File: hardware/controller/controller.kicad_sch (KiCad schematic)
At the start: 0 parts

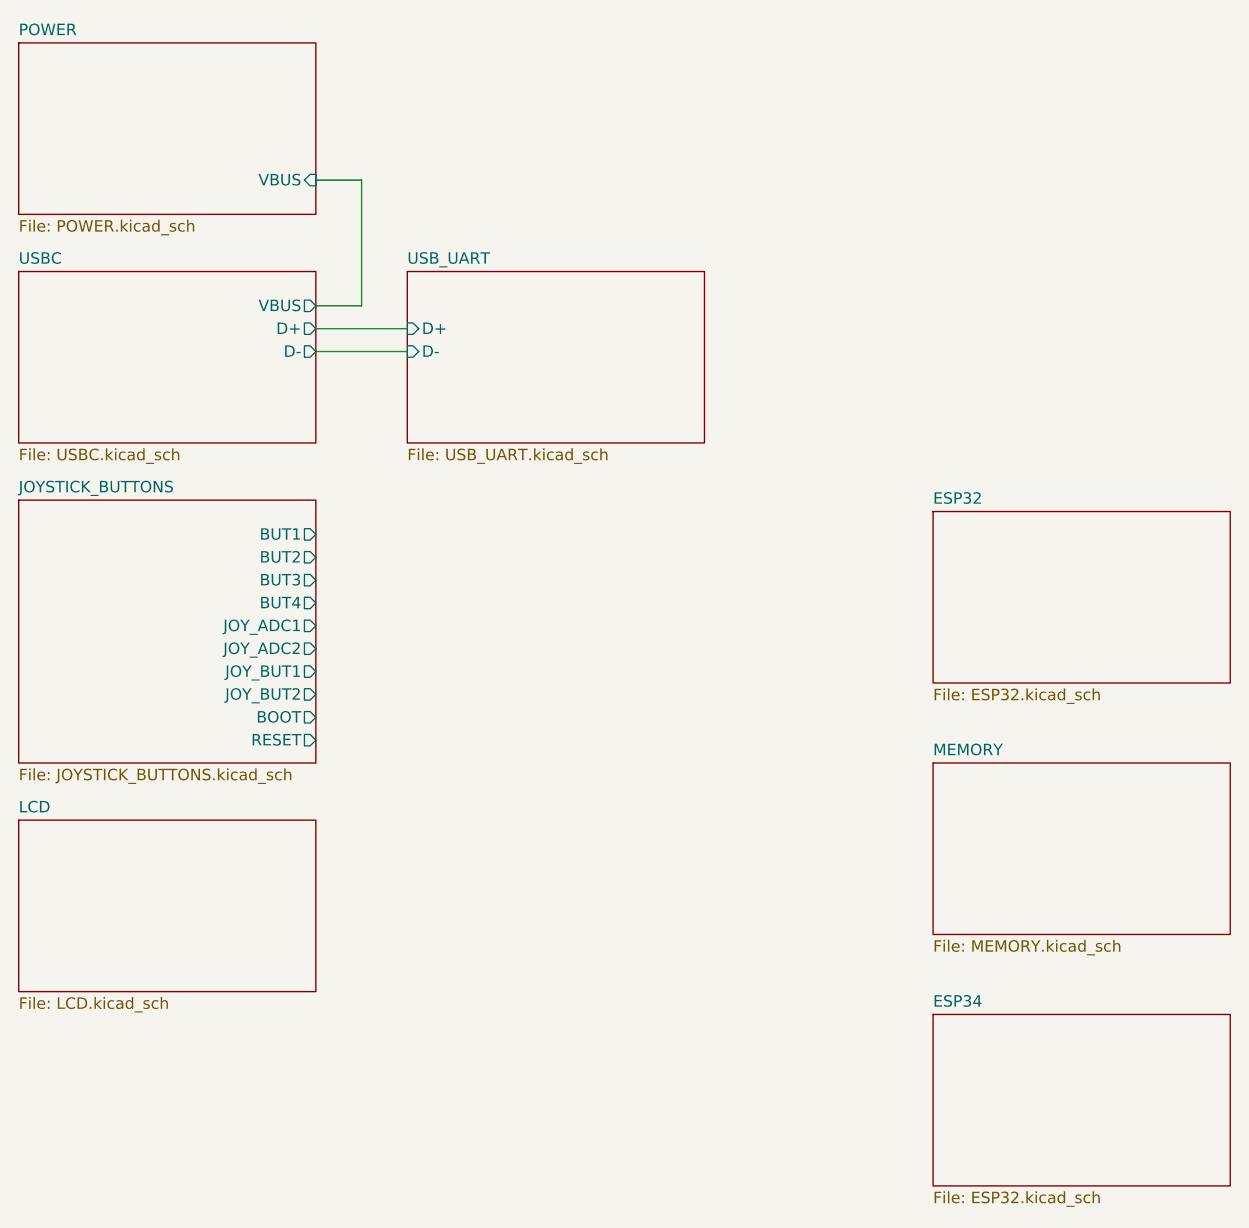
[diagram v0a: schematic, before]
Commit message: added LED IC's and USB UART bridge
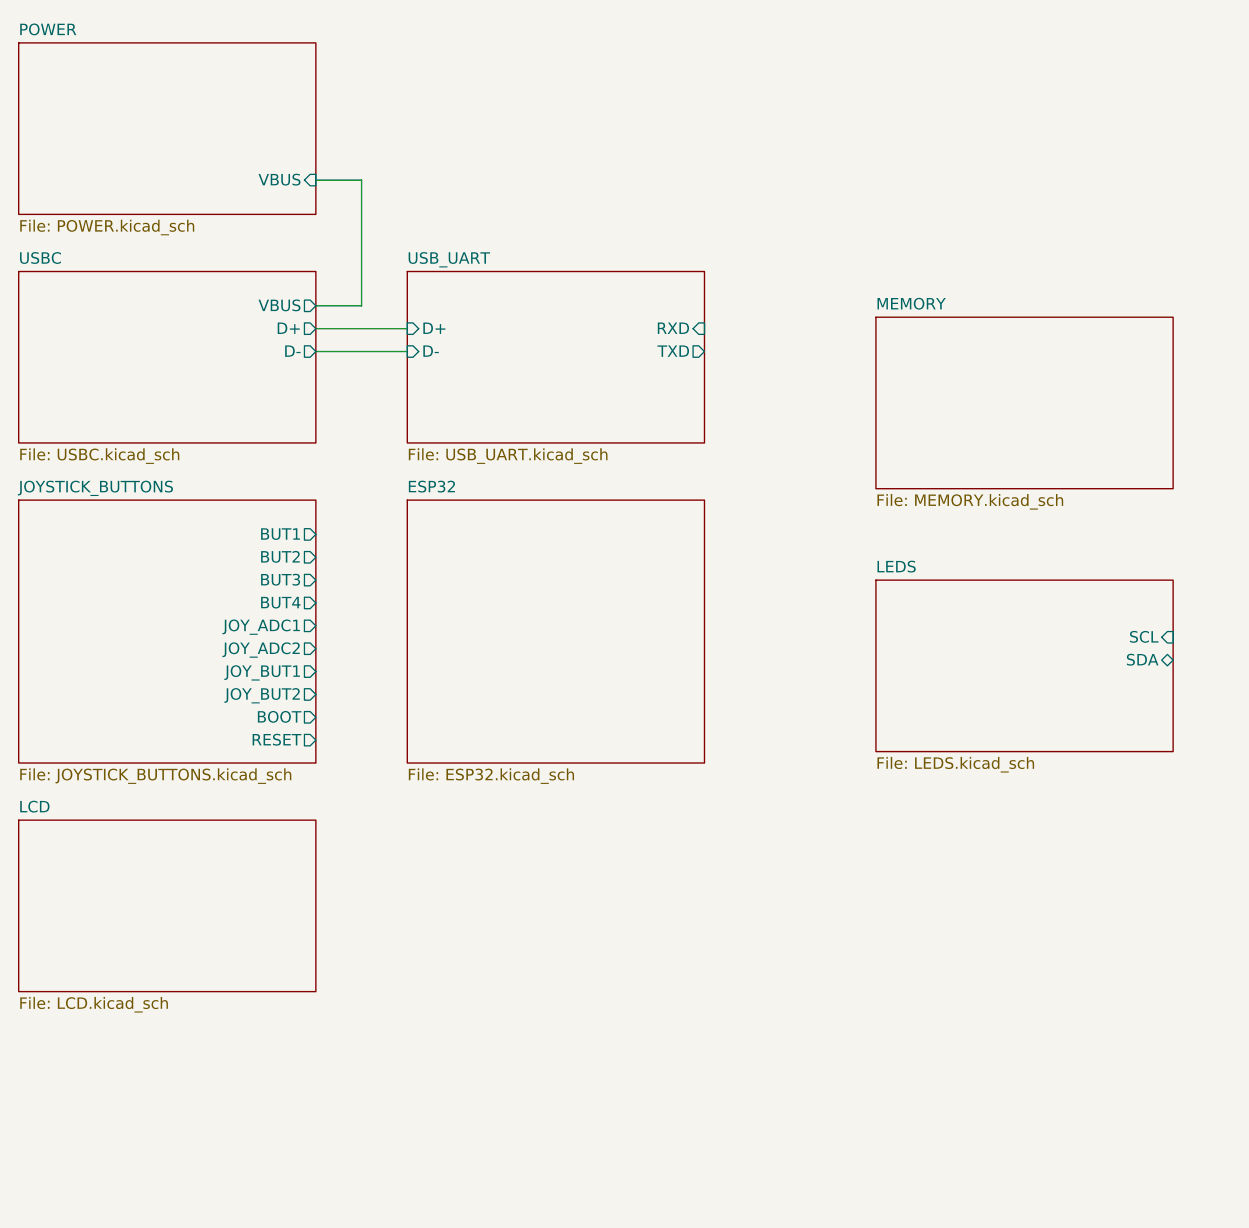
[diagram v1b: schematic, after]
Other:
- removed sheet ESP34
- added sheet LEDS (LEDS.kicad_sch)
- sheet USB_UART ports: added RXD, TXD; removed none
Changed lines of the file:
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@@
 	)
 	(sheet
-		(at 160.02 115.57)
+		(at 153.67 66.04)
 		(size 33.02 19.05)
 		(exclude_from_sim no)
@@
 		)
 		(property "Sheetname" "MEMORY"
-			(at 160.02 114.8584 0)
+			(at 153.67 65.3284 0)
 			(effects
 				(font
@@
 		)
 		(property "Sheetfile" "MEMORY.kicad_sch"
-			(at 160.02 135.2046 0)
+			(at 153.67 85.6746 0)
 			(effects
 				(font
@@
 				(path "/869bea87-c885-4ead-826b-3f34ceacafad"
 					(page "8")
+				)
+			)
+		)
+	)
+	(sheet
+		(at 153.67 95.25)
+		(size 33.02 19.05)
+		(exclude_from_sim no)
+		(in_bom yes)
+		(on_board yes)
+		(dnp no)
+		(fields_autoplaced yes)
+		(stroke
+			(width 0.1524)
+			(type solid)
+		)
+		(fill
+			(color 0 0 0 0.0000)
+		)
+		(property "Sheetname" "LEDS"
+			(at 153.67 94.5384 0)
+			(effects
+				(font
+					(size 1.27 1.27)
+				)
+				(justify left bottom)
+			)
+		)
+		(property "Sheetfile" "LEDS.kicad_sch"
+			(at 153.67 114.8846 0)
+			(effects
+				(font
+					(size 1.27 1.27)
+				)
+				(justify left top)
+			)
+		)
+		(pin "SCL" input
+			(at 186.69 101.6 0)
+			(effects
+				(font
+					(size 1.27 1.27)
+				)
+				(justify right)
+			)
+		)
+		(pin "SDA" bidirectional
+			(at 186.69 104.14 0)
+			(effects
+				(font
+					(size 1.27 1.27)
+				)
+				(justify right)
+			)
+		)
+		(instances
+			(project "controller"
+				(path "/869bea87-c885-4ead-826b-3f34ceacafad"
+					(page "9")
 				)
 			)
@@
 			)
 		)
+		(pin "RXD" input
+			(at 134.62 67.31 0)
+			(effects
+				(font
+					(size 1.27 1.27)
+				)
+				(justify right)
+			)
+		)
+		(pin "TXD" output
+			(at 134.62 69.85 0)
+			(effects
+				(font
+					(size 1.27 1.27)
+				)
+				(justify right)
+			)
+		)
 		(instances
 			(project "controller"
@@
 	)
 	(sheet
-		(at 160.02 87.63)
-		(size 33.02 19.05)
+		(at 101.6 86.36)
+		(size 33.02 29.21)
 		(exclude_from_sim no)
 		(in_bom yes)
@@
 		)
 		(property "Sheetname" "ESP32"
-			(at 160.02 86.9184 0)
+			(at 101.6 85.6484 0)
 			(effects
 				(font
@@
 		)
 		(property "Sheetfile" "ESP32.kicad_sch"
-			(at 160.02 107.2646 0)
+			(at 101.6 116.1546 0)
 			(effects
 				(font
@@
 				)
 			)
-		)
-	)
-	(sheet
-		(at 160.02 143.51)
-		(size 33.02 19.05)
-		(exclude_from_sim no)
-		(in_bom yes)
-		(on_board yes)
-		(dnp no)
-		(fields_autoplaced yes)
-		(stroke
-			(width 0.1524)
-			(type solid)
-		)
-		(fill
-			(color 0 0 0 0.0000)
-		)
-		(property "Sheetname" "ESP34"
-			(at 160.02 142.7984 0)
-			(effects
-				(font
-					(size 1.27 1.27)
-				)
-				(justify left bottom)
-			)
-		)
-		(property "Sheetfile" "ESP32.kicad_sch"
-			(at 160.02 163.1446 0)
-			(effects
-				(font
-					(size 1.27 1.27)
-				)
-				(justify left top)
-			)
-		)
-		(instances
-			(project "controller"
-				(path "/869bea87-c885-4ead-826b-3f34ceacafad"
-					(page "9")
-				)
-			)

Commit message: asdasd
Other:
- sheet JOYSTICK_BUTTONS ports: added BUT_BOOT, BUT_DWN, BUT_LFT, BUT_RHT, BUT_RST, BUT_UP, JOY1_H, JOY1_V, JOY2_H, JOY2_V; removed BOOT, BUT1, BUT2, BUT3, BUT4, JOY_ADC1, JOY_ADC2, JOY_BUT1, JOY_BUT2, RESET
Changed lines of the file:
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@@
 				)
 				(justify left top)
+				(hide yes)
 			)
 		)
@@
 				)
 				(justify left top)
+				(hide yes)
 			)
 		)
 		(pin "SCL" input
-			(at 186.69 101.6 0)
-			(effects
-				(font
-					(size 1.27 1.27)
-				)
-				(justify right)
+			(at 153.67 100.33 180)
+			(effects
+				(font
+					(size 1.27 1.27)
+				)
+				(justify left)
 			)
 		)
 		(pin "SDA" bidirectional
-			(at 186.69 104.14 0)
-			(effects
-				(font
-					(size 1.27 1.27)
-				)
-				(justify right)
+			(at 153.67 102.87 180)
+			(effects
+				(font
+					(size 1.27 1.27)
+				)
+				(justify left)
 			)
 		)
@@
 				)
 				(justify left top)
-			)
-		)
-		(pin "BUT1" output
-			(at 91.44 90.17 0)
-			(effects
-				(font
-					(size 1.27 1.27)
-				)
-				(justify right)
-			)
-		)
-		(pin "BUT2" output
-			(at 91.44 92.71 0)
-			(effects
-				(font
-					(size 1.27 1.27)
-				)
-				(justify right)
-			)
-		)
-		(pin "BUT3" output
-			(at 91.44 95.25 0)
-			(effects
-				(font
-					(size 1.27 1.27)
-				)
-				(justify right)
-			)
-		)
-		(pin "BUT4" output
-			(at 91.44 97.79 0)
-			(effects
-				(font
-					(size 1.27 1.27)
-				)
-				(justify right)
-			)
-		)
-		(pin "JOY_ADC1" output
-			(at 91.44 100.33 0)
-			(effects
-				(font
-					(size 1.27 1.27)
-				)
-				(justify right)
-			)
-		)
-		(pin "JOY_ADC2" output
-			(at 91.44 102.87 0)
-			(effects
-				(font
-					(size 1.27 1.27)
-				)
-				(justify right)
-			)
-		)
-		(pin "JOY_BUT1" output
-			(at 91.44 105.41 0)
-			(effects
-				(font
-					(size 1.27 1.27)
-				)
-				(justify right)
-			)
-		)
-		(pin "JOY_BUT2" output
-			(at 91.44 107.95 0)
-			(effects
-				(font
-					(size 1.27 1.27)
-				)
-				(justify right)
-			)
-		)
-		(pin "BOOT" output
-			(at 91.44 110.49 0)
-			(effects
-				(font
-					(size 1.27 1.27)
-				)
-				(justify right)
-			)
-		)
-		(pin "RESET" output
-			(at 91.44 113.03 0)
+				(hide yes)
+			)
+		)
+		(pin "BUT_BOOT" output
+			(at 91.44 91.44 0)
+			(effects
+				(font
+					(size 1.27 1.27)
+				)
+				(justify right)
+			)
+		)
+		(pin "BUT_DWN" output
+			(at 91.44 96.52 0)
+			(effects
+				(font
+					(size 1.27 1.27)
+				)
+				(justify right)
+			)
+		)
+		(pin "BUT_LFT" output
+			(at 91.44 99.06 0)
+			(effects
+				(font
+					(size 1.27 1.27)
+				)
+				(justify right)
+			)
+		)
+		(pin "BUT_RHT" output
+			(at 91.44 101.6 0)
+			(effects
+				(font
+					(size 1.27 1.27)
+				)
+				(justify right)
+			)
+		)
+		(pin "BUT_RST" output
+			(at 91.44 88.9 0)
+			(effects
+				(font
+					(size 1.27 1.27)
+				)
+				(justify right)
+			)
+		)
+		(pin "BUT_UP" output
+			(at 91.44 93.98 0)
+			(effects
+				(font
+					(size 1.27 1.27)
+				)
+				(justify right)
+			)
+		)
+		(pin "JOY1_H" output
+			(at 91.44 104.14 0)
+			(effects
+				(font
+					(size 1.27 1.27)
+				)
+				(justify right)
+			)
+		)
+		(pin "JOY1_V" output
+			(at 91.44 106.68 0)
+			(effects
+				(font
+					(size 1.27 1.27)
+				)
+				(justify right)
+			)
+		)
+		(pin "JOY2_H" output
+			(at 91.44 109.22 0)
+			(effects
+				(font
+					(size 1.27 1.27)
+				)
+				(justify right)
+			)
+		)
+		(pin "JOY2_V" output
+			(at 91.44 111.76 0)
 			(effects
 				(font
@@
 				)
 				(justify left top)
+				(hide yes)
 			)
 		)
@@
 				)
 				(justify left top)
+				(hide yes)
 			)
 		)
@@
 				)
 				(justify left top)
+				(hide yes)
 			)
 		)
@@
 	)
 	(sheet
-		(at 58.42 121.92)
+		(at 153.67 120.65)
 		(size 33.02 19.05)
 		(exclude_from_sim no)
@@
 		)
 		(property "Sheetname" "LCD"
-			(at 58.42 121.2084 0)
+			(at 153.67 119.9384 0)
 			(effects
 				(font
@@
 		)
 		(property "Sheetfile" "LCD.kicad_sch"
-			(at 58.42 141.5546 0)
-			(effects
-				(font
-					(size 1.27 1.27)
-				)
-				(justify left top)
+			(at 153.67 140.2846 0)
+			(effects
+				(font
+					(size 1.27 1.27)
+				)
+				(justify left top)
+				(hide yes)
 			)
 		)
@@
 				)
 				(justify left top)
-			)
-		)
+				(hide yes)
+			)
+		)

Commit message: a
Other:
- sheet ESP32 ports: added BUT_JOY{BUT_JOY_BUS}, DTR, RTS, RXD, SCL, SDA, TXD; removed none
- sheet JOYSTICK_BUTTONS ports: added BUT_JOY{BUT_JOY_BUS}; removed BUT_BOOT, BUT_DWN, BUT_LFT, BUT_RHT, BUT_RST, BUT_UP, JOY1_H, JOY1_V, JOY2_H, JOY2_V
- sheet LCD ports: added I2C_LCD, SPI_LCD; removed none
- sheet USBC ports: added USB+, USB-; removed D+, D-
- sheet USB_UART ports: added DTR, RTS, USB+, USB-, VBUS; removed D+, D-

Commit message: fixed bus stuff
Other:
- added sheet SPEAKER (SPEAKER.kicad_sch)
- sheet ESP32 ports: added I2C_CTP_LED{I2C_CTP_LED}, SPI_LCD_SD{SPI_LCD_SD}; removed SCL, SDA
- sheet LCD ports: added I2C_CTP_LED{I2C_CTP_LED}, SPI_LCD_SD{SPI_LCD_SD}; removed I2C_LCD, SPI_LCD
- sheet LEDS ports: added GPIO, I2C_CTP_LED{I2C_CTP_LED}; removed SCL, SDA
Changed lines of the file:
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@@
+	)
+	(junction
+		(at 151.13 105.41)
+		(diameter 0)
+		(color 0 0 0 0)
 	)
 	(junction
@@
 		(color 0 0 0 0)
 	)
+	(bus
+		(pts
+			(xy 151.13 105.41) (xy 151.13 120.65)
+		)
+		(stroke
+			(width 0)
+			(type default)
+		)
+	)
 	(wire
 		(pts
@@
 	(wire
 		(pts
-			(xy 134.62 96.52) (xy 154.94 96.52)
-		)
-		(stroke
-			(width 0)
-			(type default)
-		)
-	)
-	(wire
-		(pts
 			(xy 123.19 80.01) (xy 123.19 86.36)
 		)
@@
 		)
 	)
+	(bus
+		(pts
+			(xy 148.59 123.19) (xy 154.94 123.19)
+		)
+		(stroke
+			(width 0)
+			(type default)
+		)
+	)
+	(bus
+		(pts
+			(xy 154.94 100.33) (xy 151.13 100.33)
+		)
+		(stroke
+			(width 0)
+			(type default)
+		)
+	)
+	(bus
+		(pts
+			(xy 134.62 107.95) (xy 148.59 107.95)
+		)
+		(stroke
+			(width 0)
+			(type default)
+		)
+	)
 	(wire
 		(pts
@@
 		)
 	)
-	(wire
-		(pts
-			(xy 134.62 93.98) (xy 154.94 93.98)
-		)
-		(stroke
-			(width 0)
-			(type default)
-		)
-	)
 	(bus
 		(pts
@@
 		)
 	)
+	(bus
+		(pts
+			(xy 151.13 120.65) (xy 154.94 120.65)
+		)
+		(stroke
+			(width 0)
+			(type default)
+		)
+	)
+	(bus
+		(pts
+			(xy 148.59 107.95) (xy 148.59 123.19)
+		)
+		(stroke
+			(width 0)
+			(type default)
+		)
+	)
+	(bus
+		(pts
+			(xy 134.62 105.41) (xy 151.13 105.41)
+		)
+		(stroke
+			(width 0)
+			(type default)
+		)
+	)
 	(wire
 		(pts
@@
 		(pts
 			(xy 96.52 64.77) (xy 96.52 50.8)
+		)
+		(stroke
+			(width 0)
+			(type default)
+		)
+	)
+	(bus
+		(pts
+			(xy 151.13 100.33) (xy 151.13 105.41)
 		)
 		(stroke
@@
 			)
 		)
-		(pin "SCL" bidirectional
-			(at 154.94 93.98 180)
-			(effects
-				(font
-					(size 1.27 1.27)
-				)
-				(justify left)
-			)
-		)
-		(pin "SDA" bidirectional
-			(at 154.94 96.52 180)
+		(pin "GPIO" input
+			(at 154.94 97.79 180)
+			(effects
+				(font
+					(size 1.27 1.27)
+				)
+				(justify left)
+			)
+		)
+		(pin "I2C_CTP_LED{I2C_CTP_LED}" bidirectional
+			(at 154.94 100.33 180)
 			(effects
 				(font
@@
 			)
 		)
-		(pin "SCL" bidirectional
-			(at 134.62 93.98 0)
-			(effects
-				(font
-					(size 1.27 1.27)
-				)
-				(justify right)
-			)
-		)
-		(pin "SDA" bidirectional
-			(at 134.62 96.52 0)
-			(effects
-				(font
-					(size 1.27 1.27)
-				)
-				(justify right)
-			)
-		)
 		(pin "RXD" output
 			(at 125.73 86.36 90)
@@
 		(pin "DTR" input
 			(at 123.19 86.36 90)
+			(effects
+				(font
+					(size 1.27 1.27)
+				)
+				(justify right)
+			)
+		)
+		(pin "I2C_CTP_LED{I2C_CTP_LED}" bidirectional
+			(at 134.62 105.41 0)
+			(effects
+				(font
+					(size 1.27 1.27)
+				)
+				(justify right)
+			)
+		)
+		(pin "SPI_LCD_SD{SPI_LCD_SD}" bidirectional
+			(at 134.62 107.95 0)
 			(effects
 				(font
@@
 			)
 		)
-		(pin "I2C_LCD" bidirectional
-			(at 154.94 121.92 180)
-			(effects
-				(font
-					(size 1.27 1.27)
-				)
-				(justify left)
-			)
-		)
-		(pin "SPI_LCD" bidirectional
-			(at 154.94 125.73 180)
+		(pin "I2C_CTP_LED{I2C_CTP_LED}" bidirectional
+			(at 154.94 120.65 180)
+			(effects
+				(font
+					(size 1.27 1.27)
+				)
+				(justify left)
+			)
+		)
+		(pin "SPI_LCD_SD{SPI_LCD_SD}" bidirectional
+			(at 154.94 123.19 180)
 			(effects
 				(font
@@
 				)
 			)
+		)
+	)
+	(sheet
+		(at 58.42 120.65)
+		(size 33.02 21.59)
+		(exclude_from_sim no)
+		(in_bom yes)
+		(on_board yes)
+		(dnp no)
+		(fields_autoplaced yes)
+		(stroke
+			(width 0.1524)
+			(type solid)
+		)
+		(fill
+			(color 0 0 0 0.0000)
+		)
+		(property "Sheetname" "SPEAKER"
+			(at 58.42 119.9384 0)
+			(effects
+				(font
+					(size 1.27 1.27)
+				)
+				(justify left bottom)
+			)
+		)
+		(property "Sheetfile" "SPEAKER.kicad_sch"
+			(at 58.42 142.8246 0)
+			(effects
+				(font
+					(size 1.27 1.27)
+				)
+				(justify left top)
+			)
+		)
+		(instances
+			(project "controller"
+				(path "/869bea87-c885-4ead-826b-3f34ceacafad"
+					(page "10")
+				)
+			)

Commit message: bussin
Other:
- removed sheet SPEAKER
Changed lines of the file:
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@@
-	)
-	(sheet
-		(at 58.42 120.65)
-		(size 33.02 21.59)
-		(exclude_from_sim no)
-		(in_bom yes)
-		(on_board yes)
-		(dnp no)
-		(fields_autoplaced yes)
-		(stroke
-			(width 0.1524)
-			(type solid)
-		)
-		(fill
-			(color 0 0 0 0.0000)
-		)
-		(property "Sheetname" "SPEAKER"
-			(at 58.42 119.9384 0)
-			(effects
-				(font
-					(size 1.27 1.27)
-				)
-				(justify left bottom)
-			)
-		)
-		(property "Sheetfile" "SPEAKER.kicad_sch"
-			(at 58.42 142.8246 0)
-			(effects
-				(font
-					(size 1.27 1.27)
-				)
-				(justify left top)
-			)
-		)
-		(instances
-			(project "controller"
-				(path "/869bea87-c885-4ead-826b-3f34ceacafad"
-					(page "10")
-				)
-			)
-		)
 	)
 	(sheet

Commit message: added memory and fixed gpio pins
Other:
- sheet ESP32 ports: added LED_GPIO, MEM{MEMORY}; removed none
- sheet LEDS ports: added LED GPIO; removed GPIO
- sheet MEMORY ports: added MEM{MEMORY}; removed none
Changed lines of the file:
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@@
+	(bus
+		(pts
+			(xy 134.62 127) (xy 139.7 127)
+		)
+		(stroke
+			(width 0)
+			(type default)
+		)
+	)
 	(bus
 		(pts
@@
 		)
 	)
+	(bus
+		(pts
+			(xy 139.7 127) (xy 139.7 110.49)
+		)
+		(stroke
+			(width 0)
+			(type default)
+		)
+	)
 	(wire
 		(pts
@@
 		)
 	)
+	(wire
+		(pts
+			(xy 134.62 97.79) (xy 154.94 97.79)
+		)
+		(stroke
+			(width 0)
+			(type default)
+		)
+	)
 	(bus
 		(pts
@@
 		(pts
 			(xy 125.73 80.01) (xy 125.73 86.36)
+		)
+		(stroke
+			(width 0)
+			(type default)
+		)
+	)
+	(bus
+		(pts
+			(xy 139.7 110.49) (xy 134.62 110.49)
 		)
 		(stroke
@@
 	(sheet
 		(at 102.235 123.19)
-		(size 33.02 19.05)
+		(size 32.385 19.05)
 		(exclude_from_sim no)
 		(in_bom yes)
@@
 				(justify left top)
 				(hide yes)
+			)
+		)
+		(pin "MEM{MEMORY}" bidirectional
+			(at 134.62 127 0)
+			(effects
+				(font
+					(size 1.27 1.27)
+				)
+				(justify right)
 			)
 		)
@@
 			)
 		)
-		(pin "GPIO" input
-			(at 154.94 97.79 180)
-			(effects
-				(font
-					(size 1.27 1.27)
-				)
-				(justify left)
-			)
-		)
 		(pin "I2C_CTP_LED{I2C_CTP_LED}" bidirectional
 			(at 154.94 100.33 180)
+			(effects
+				(font
+					(size 1.27 1.27)
+				)
+				(justify left)
+			)
+		)
+		(pin "LED GPIO" input
+			(at 154.94 97.79 180)
 			(effects
 				(font
@@
 			(effects
 				(font
+					(size 1.27 1.27)
+				)
+				(justify right)
+			)
+		)
+		(pin "LED_GPIO" output
+			(at 134.62 97.79 0)
+			(effects
+				(font
+					(size 1.27 1.27)
+				)
+				(justify right)
+			)
+		)
+		(pin "MEM{MEMORY}" bidirectional
+			(at 134.62 110.49 0)
+			(effects
+				(font
